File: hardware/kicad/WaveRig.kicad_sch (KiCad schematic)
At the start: 0 parts

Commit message: Remove pins from power hierarchial sheet, not needed.
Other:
- sheet Power ports: added none; removed 5V_HOST, VBUS_5V
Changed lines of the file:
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@@
-	(wire
-		(pts
-			(xy 50 43.81) (xy 55.08 43.81)
-		)
-		(stroke
-			(width 0)
-			(type default)
-		)
-	)
 	(wire
 		(pts
@@
 		(pts
 			(xy 120 103.97) (xy 114.92 103.97)
-		)
-		(stroke
-			(width 0)
-			(type default)
-		)
-	)
-	(wire
-		(pts
-			(xy 20 43.81) (xy 14.92 43.81)
 		)
 		(stroke
@@
 		)
 	)
-	(label "VBUS_5V"
-		(at 14.92 43.81 0)
-		(effects
-			(font
-				(size 1.27 1.27)
-			)
-			(justify left bottom)
-		)
-	)
 	(label "USB_D-"
 		(at 155.08 48.89 0)
@@
 	(label "VBUS_5V"
 		(at 155.08 43.81 0)
-		(effects
-			(font
-				(size 1.27 1.27)
-			)
-			(justify left bottom)
-		)
-	)
-	(label "5V_HOST"
-		(at 55.08 43.81 0)
 		(effects
 			(font
@@
 			)
 		)
-		(pin "VBUS_5V" input
-			(at 20 43.81 180)
-			(effects
-				(font
-					(size 1.27 1.27)
-				)
-				(justify right)
-			)
-		)
-		(pin "5V_HOST" output
-			(at 50 43.81 0)
-			(effects
-				(font
-					(size 1.27 1.27)
-				)
-				(justify right)
-			)
-		)

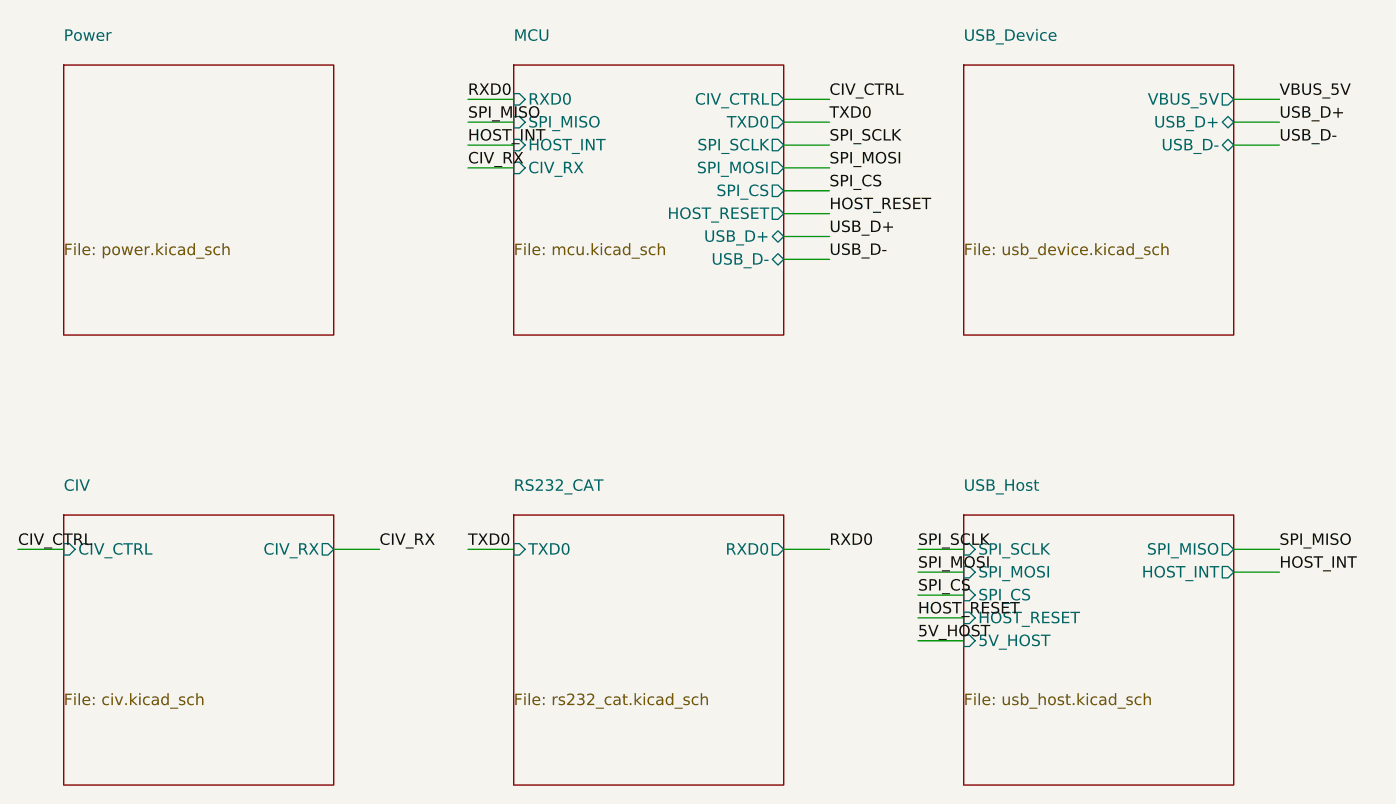
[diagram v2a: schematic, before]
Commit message: Refactor the microcontroller sheet; add switch footprint and 3d file; add titles, date and WaveRig annotation to all sheets.
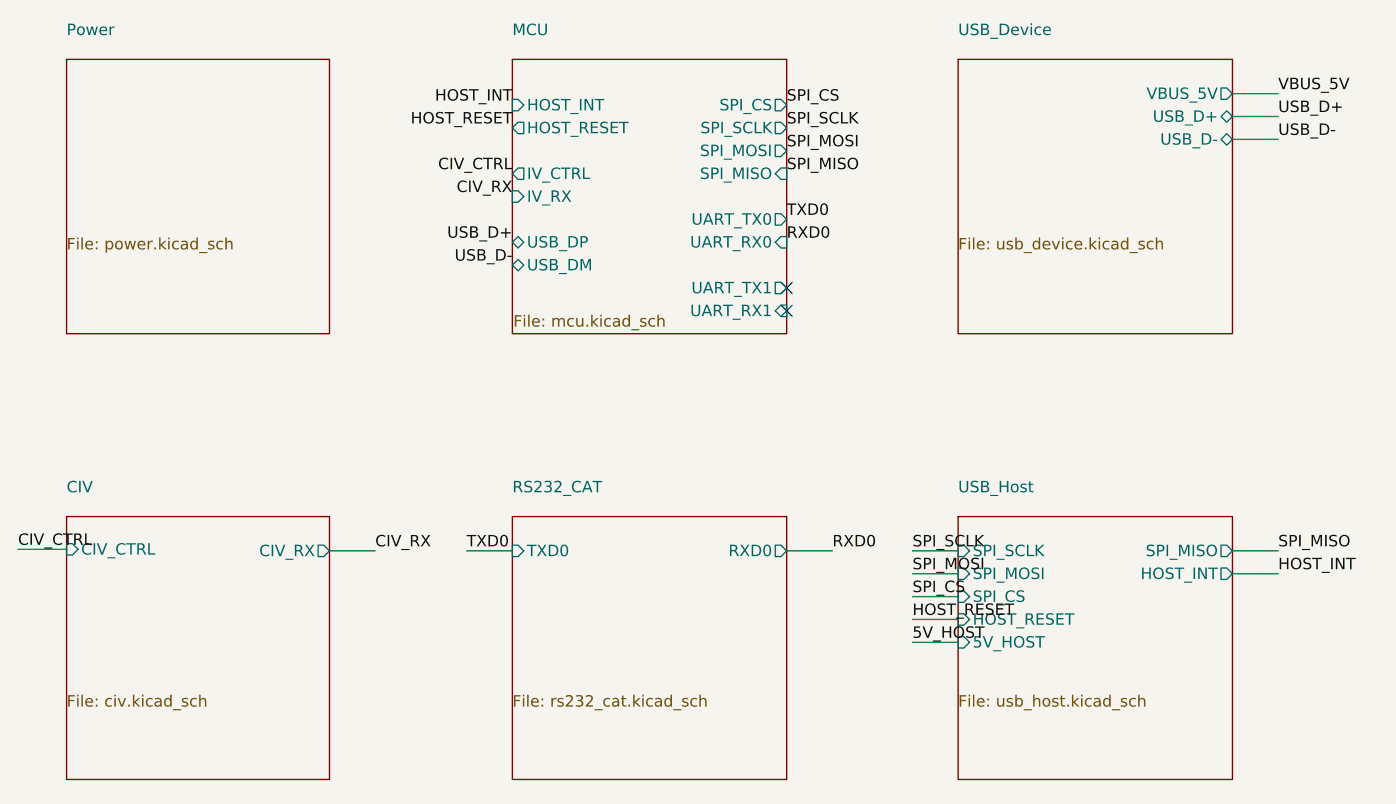
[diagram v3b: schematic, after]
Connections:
- no-connect marks 0 -> 2
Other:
- sheet MCU ports: added IV_CTRL, IV_RX, UART_RX0, UART_RX1, UART_TX0, UART_TX1, USB_DM, USB_DP; removed CIV_CTRL, CIV_RX, RXD0, TXD0, USB_D+, USB_D-
- company: (none) -> WaveRig
- title: (none) -> Parent Sheet

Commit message: Refactor the USB connector sheet.
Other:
- sheet USB_Device ports: added USB_DM, USB_DP; removed USB_D+, USB_D-, VBUS_5V
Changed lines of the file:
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@@
-		)
-	)
-	(wire
-		(pts
-			(xy 149.86 43.18) (xy 154.94 43.18)
-		)
-		(stroke
-			(width 0)
-			(type default)
 		)
 	)
@@
 	(label "SPI_MISO"
 		(at 100.33 52.07 0)
-		(effects
-			(font
-				(size 1.27 1.27)
-			)
-			(justify left bottom)
-		)
-	)
-	(label "VBUS_5V"
-		(at 154.94 43.18 0)
 		(effects
 			(font
@@
 			)
 		)
-		(pin "VBUS_5V" output
-			(at 149.86 43.18 0)
-			(effects
-				(font
-					(size 1.27 1.27)
-				)
-				(justify right)
-			)
-		)
-		(pin "USB_D+" bidirectional
+		(pin "USB_DM" bidirectional
+			(at 149.86 48.26 0)
+			(effects
+				(font
+					(size 1.27 1.27)
+				)
+				(justify right)
+			)
+		)
+		(pin "USB_DP" bidirectional
 			(at 149.86 45.72 0)
 			(effects
 				(font
-					(size 1.27 1.27)
-				)
-				(justify right)
-			)
-		)
-		(pin "USB_D-" bidirectional
-			(at 149.86 48.26 0)
-			(effects
-				(font
